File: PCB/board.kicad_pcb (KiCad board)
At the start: 2 copper layers, 161 parts, among them J1 Micro_SD_Card, J10 Conn_01x10, J11 Conn_01x02, J12 Conn_02x04_Odd_Even, J13 Conn_01x02, J14 Conn_01x02, J15 Conn_01x03, J16 Conn_01x02, J17 Conn_01x05, J18 Conn_01x04, J19 Conn_01x04, J2 Conn_ARM_JTAG_SWD_10, J20 Conn_01x02, J21 Conn_01x03, J22 Conn_02x04_Odd_Even, J23 Conn_01x04, J24 Conn_01x04, J25 Conn_01x02, J26 Conn_01x03, J27 Conn_02x04_Odd_Even, J28 Conn_01x04, J29 Conn_01x04, J3 USB_C_Receptacle_USB2.0_14P, J30 Conn_01x02, J31 Conn_01x03, J32 Conn_01x02, J33 Conn_01x02, J34 Conn_01x02, J35 Conn_01x02, J36 Conn_01x02, J37 Conn_01x02, J4 Conn_01x04, J5 Conn_01x04, J6 Conn_01x02, J7 Conn_01x03, J8 Conn_02x04_Odd_Even, J9 Conn_01x10, Q1 IRLML6402, Q2 NMOS, Q3 NMOS, Q4 NMOS, Q5 NMOS, Q6 NMOS, SW1 SW_Push, SW2 SW_Push, U1 STM32H743VITx, U2 AP7361C, U4 TMC Stepstick, U5 TMC Stepstick, U6 TMC Stepstick, U7 TMC Stepstick, U8 AP63203WU, Y2 25 MHz

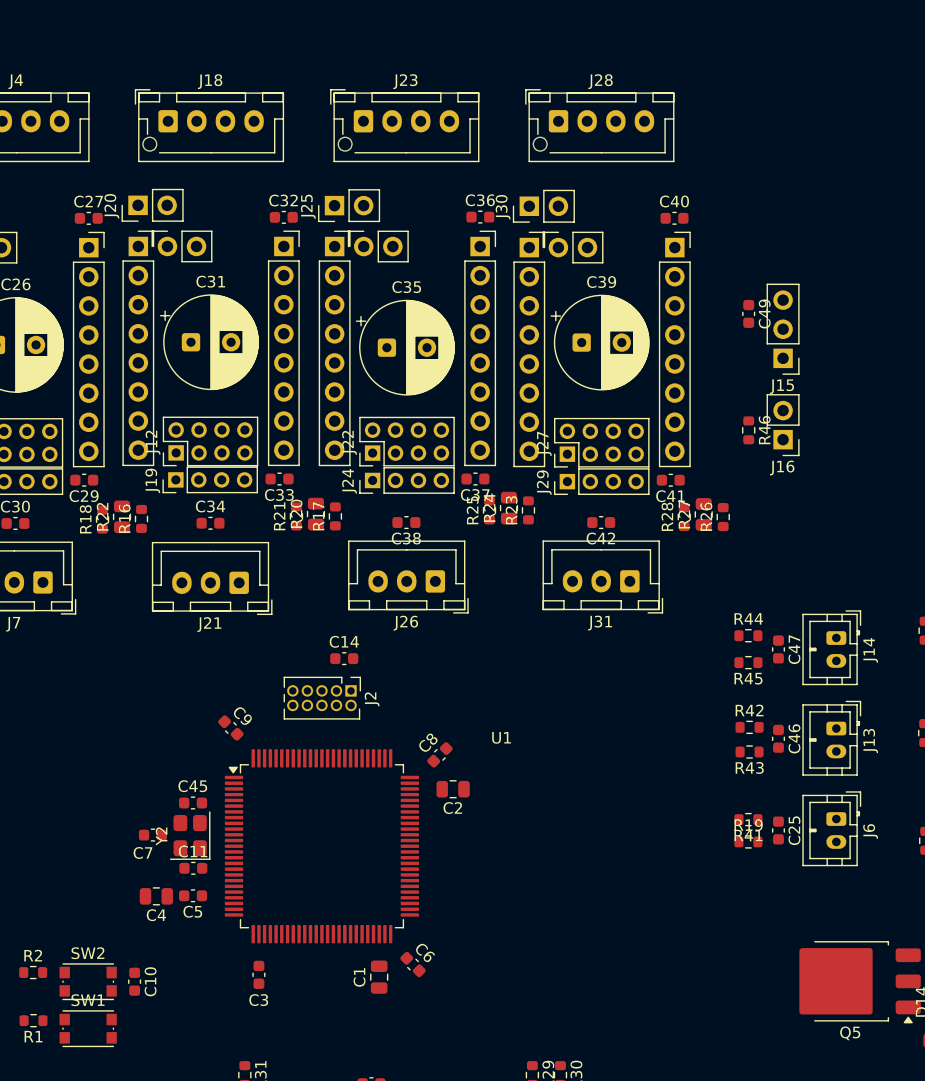
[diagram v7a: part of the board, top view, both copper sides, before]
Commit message: starting to compress everything now, motor drivers and mcu down
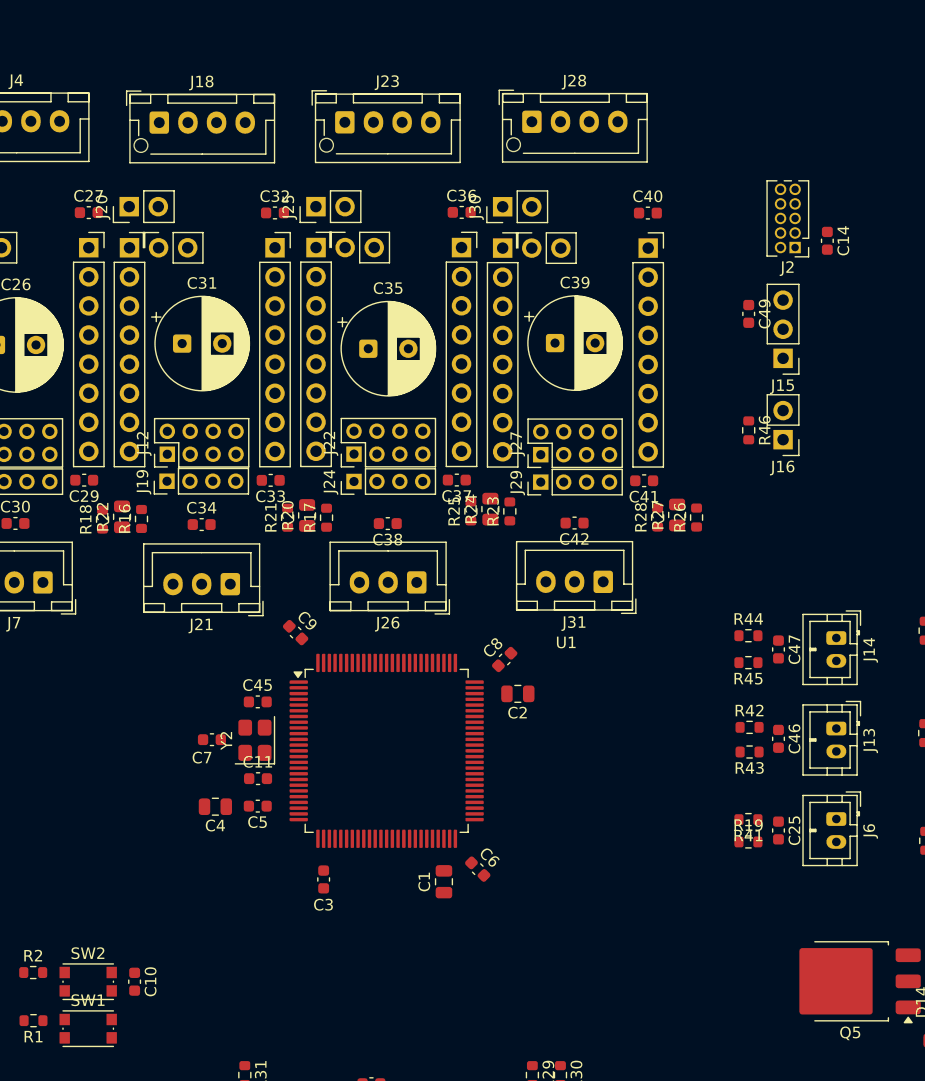
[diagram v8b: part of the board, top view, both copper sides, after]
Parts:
- moved C14 55.7 mm to (235.2, 39.1), turned to -90 degrees
- moved J2 54.8 mm to (232.4, 39.7), turned to 180 degrees
- moved C45 10.5 mm to (185.5, 79.3)
- moved C3 10.1 mm to (191.2, 94.8)
- moved C8 10.1 mm to (207.1, 75.6)
- moved U1 10.1 mm to (196.8, 83.6)
- moved Y2 10.1 mm to (185.2, 82.7)
- moved C1 10.1 mm to (201.8, 95.0)
- moved C9 10.1 mm to (188.8, 73.3)
- moved C2 10.1 mm to (208.2, 78.6)
- moved C6 10.1 mm to (204.7, 93.9)
- moved C7 9.79 mm to (181.5, 82.6)
- moved C5 9.65 mm to (185.5, 88.4)
- moved C11 9.65 mm to (185.5, 86.0)
- moved C4 9.37 mm to (181.8, 88.5)
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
